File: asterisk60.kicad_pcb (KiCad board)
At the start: 2 copper layers, 227.3 x 95.2 mm, 125 parts, among them SW0 MX_LED, SW1 MX_LED, SW10 MX_LED, SW11 MX_LED, SW12 MX_LED, SW13 MX_LED, SW14 MX_LED, SW15 MX_LED, SW16 MX_LED, SW17 MX_LED, SW18 MX_LED, SW19 MX_LED, SW2 MX_LED, SW20 MX_LED, SW21 MX_LED, SW22 MX_LED, SW23 MX_LED, SW24 MX_LED, SW25 MX_LED, SW26 MX_LED, SW27 MX_LED, SW28 MX_LED, SW29 MX_LED, SW3 MX_LED, SW30 MX_LED, SW31 MX_LED, SW32 MX_LED, SW33 MX_LED, SW34 MX_LED, SW35 MX_LED, SW36 MX_LED, SW37 MX_LED, SW38 MX_LED, SW39 MX_LED, SW4 MX_LED, SW40 MX_LED, SW41 MX_LED, SW42 MX_LED, SW43 MX_LED, SW44 MX_LED, SW45 MX_LED, SW46 MX_LED, SW47 MX_LED, SW48 MX_LED, SW49 MX_LED, SW5 MX_LED, SW50 MX_LED, SW51 MX_LED, SW52 MX_LED, SW53 MX_LED, SW54 MX_LED, SW55 MX_LED, SW56 MX_LED, SW57 MX_LED, SW58 MX_LED, SW59 MX_LED, SW6 MX_LED, SW7 MX_LED, SW8 MX_LED, SW9 MX_LED, U1 ProMicro

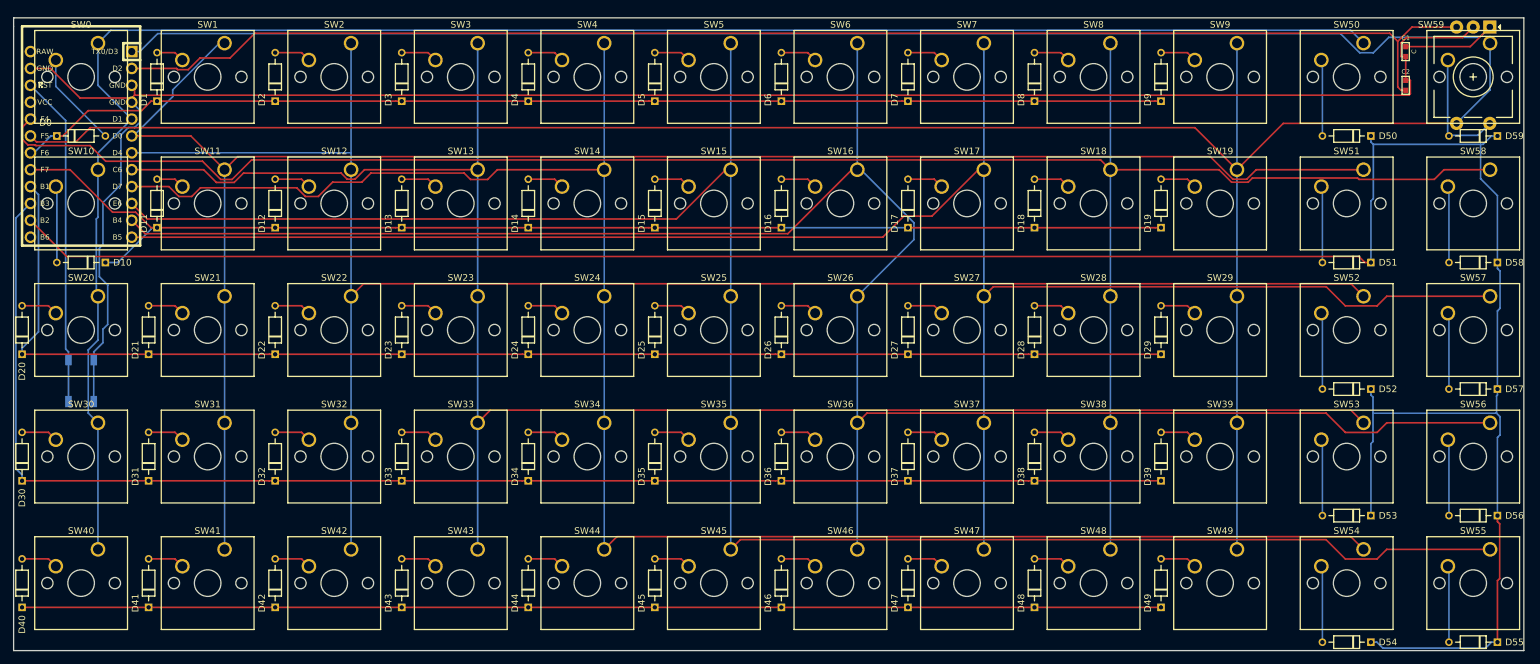
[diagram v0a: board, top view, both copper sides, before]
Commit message: revamped pcb and added top and bottom plates
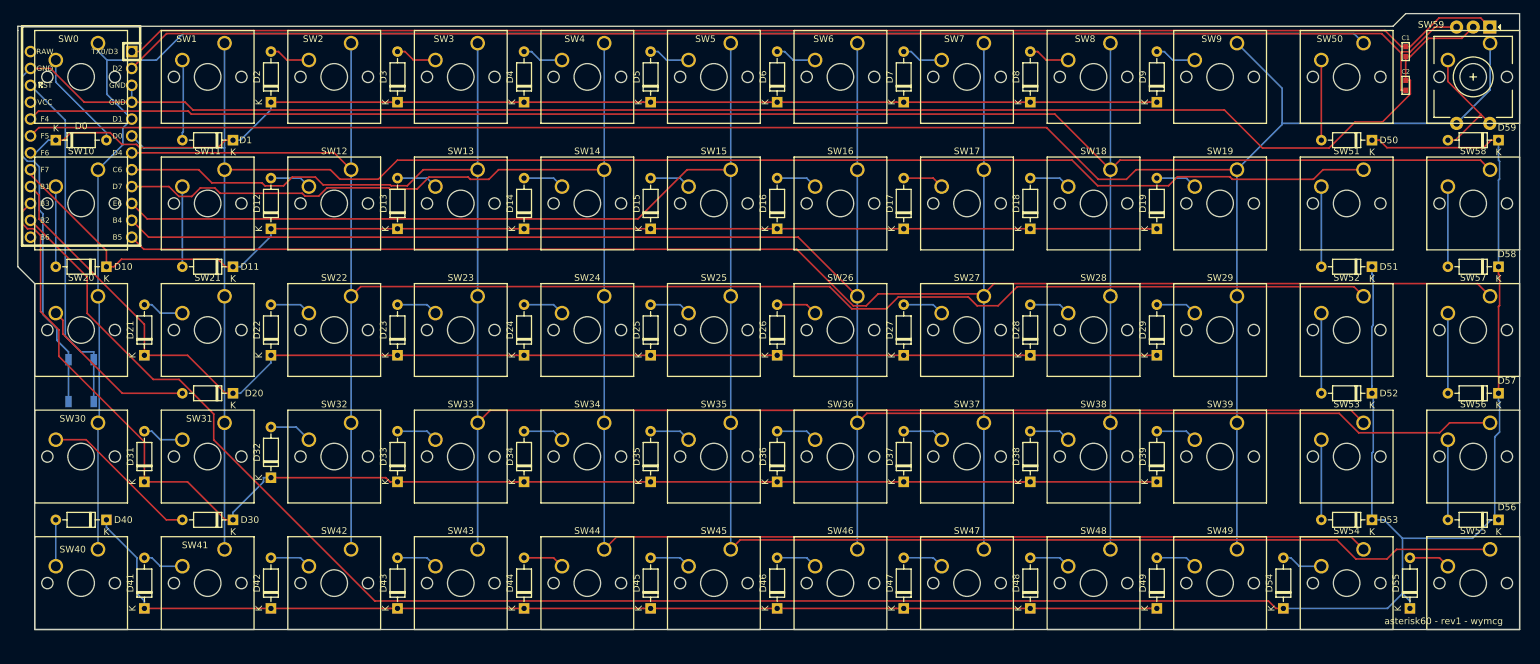
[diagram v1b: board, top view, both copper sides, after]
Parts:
- D0, D1, D10, D11, D12, D13, D14, D15, D16, D17, D18, D19, D2, D20, D21, D22, D23, D24, D25, D26, D27, D28, D29, D3, D30, D31, D32, D33, D34, D35, D36, D37, D38, D39, D4, D40, D41, D42, D43, D44, D45, D46, D47, D48, D49, D5, D50, D51, D52, D53, D54, D55, D56, D57, D58, D59, D6, D7, D8, D9: footprint diode:Diotec_Semiconductor-1N4148-0 -> Diode_THT:D_DO-35_SOD27_P7.62mm_Horizontal
- moved D20 33.1 mm to (58.4, 83.2), turned to 180 degrees
- moved D30 33.1 mm to (58.4, 102.2), turned to 180 degrees
- moved D40 15.9 mm to (39.4, 102.2), turned to 180 degrees
- moved D11 14.9 mm to (58.4, 64.1), turned to 180 degrees
- moved D1 14.9 mm to (58.4, 45.1), turned to 180 degrees
- moved D54 10.8 mm to (216.5, 115.6), turned to 90 degrees
- moved D55 10.8 mm to (235.6, 115.6), turned to 90 degrees
- moved D17 3.86 mm to (159.4, 58.4)
- moved D27 3.86 mm to (159.4, 77.5)
- moved D37 3.86 mm to (159.4, 96.5)
- moved D14 3.86 mm to (102.2, 58.4)
- moved D15 3.86 mm to (121.3, 58.4)
- moved D24 3.86 mm to (102.2, 77.5)
- moved D25 3.86 mm to (121.3, 77.5)
- moved D34 3.86 mm to (102.2, 96.5)
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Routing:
- net Net-(D20-Pad2): track 5.54 -> 25.2 mm
- net Net-(D30-Pad2): track 5.54 -> 24.0 mm
- net ROT0: track 222.2 -> 209.1 mm
- net R5: track 377.7 -> 386.2 mm
- net GND: track 283.1 -> 291.0 mm
- net R2: track 198.2 -> 190.3 mm
- net Net-(D1-Pad2): track 4.27 -> 12.2 mm
- net Net-(D11-Pad2): track 4.27 -> 12.1 mm
- net C6: track 295.3 -> 287.8 mm
- net C8: track 306.8 -> 301.3 mm
- net Net-(D55-Pad2): track 11.5 -> 6.24 mm
- net Net-(D54-Pad2): track 11.5 -> 6.24 mm
- net R3: track 214.5 -> 209.3 mm
- net C2: track 263.2 -> 267.7 mm
- net C9: track 311.8 -> 308.2 mm
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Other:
- board size 227.3 x 95.2 mm -> 226.1 x 92.7 mm
- board text added: "asterisk60 - rev1 - wymcg"

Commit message: logo added
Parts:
- added REF**: origami-logo-eighth, customlogos:origami-logo-eighth, F.Cu at (238.1, 115.6)
- added REF**: origami-logo-eighth, customlogos:origami-logo-eighth, B.Cu at (223.5, 115.6)
